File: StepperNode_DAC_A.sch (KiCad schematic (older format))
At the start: 1 part

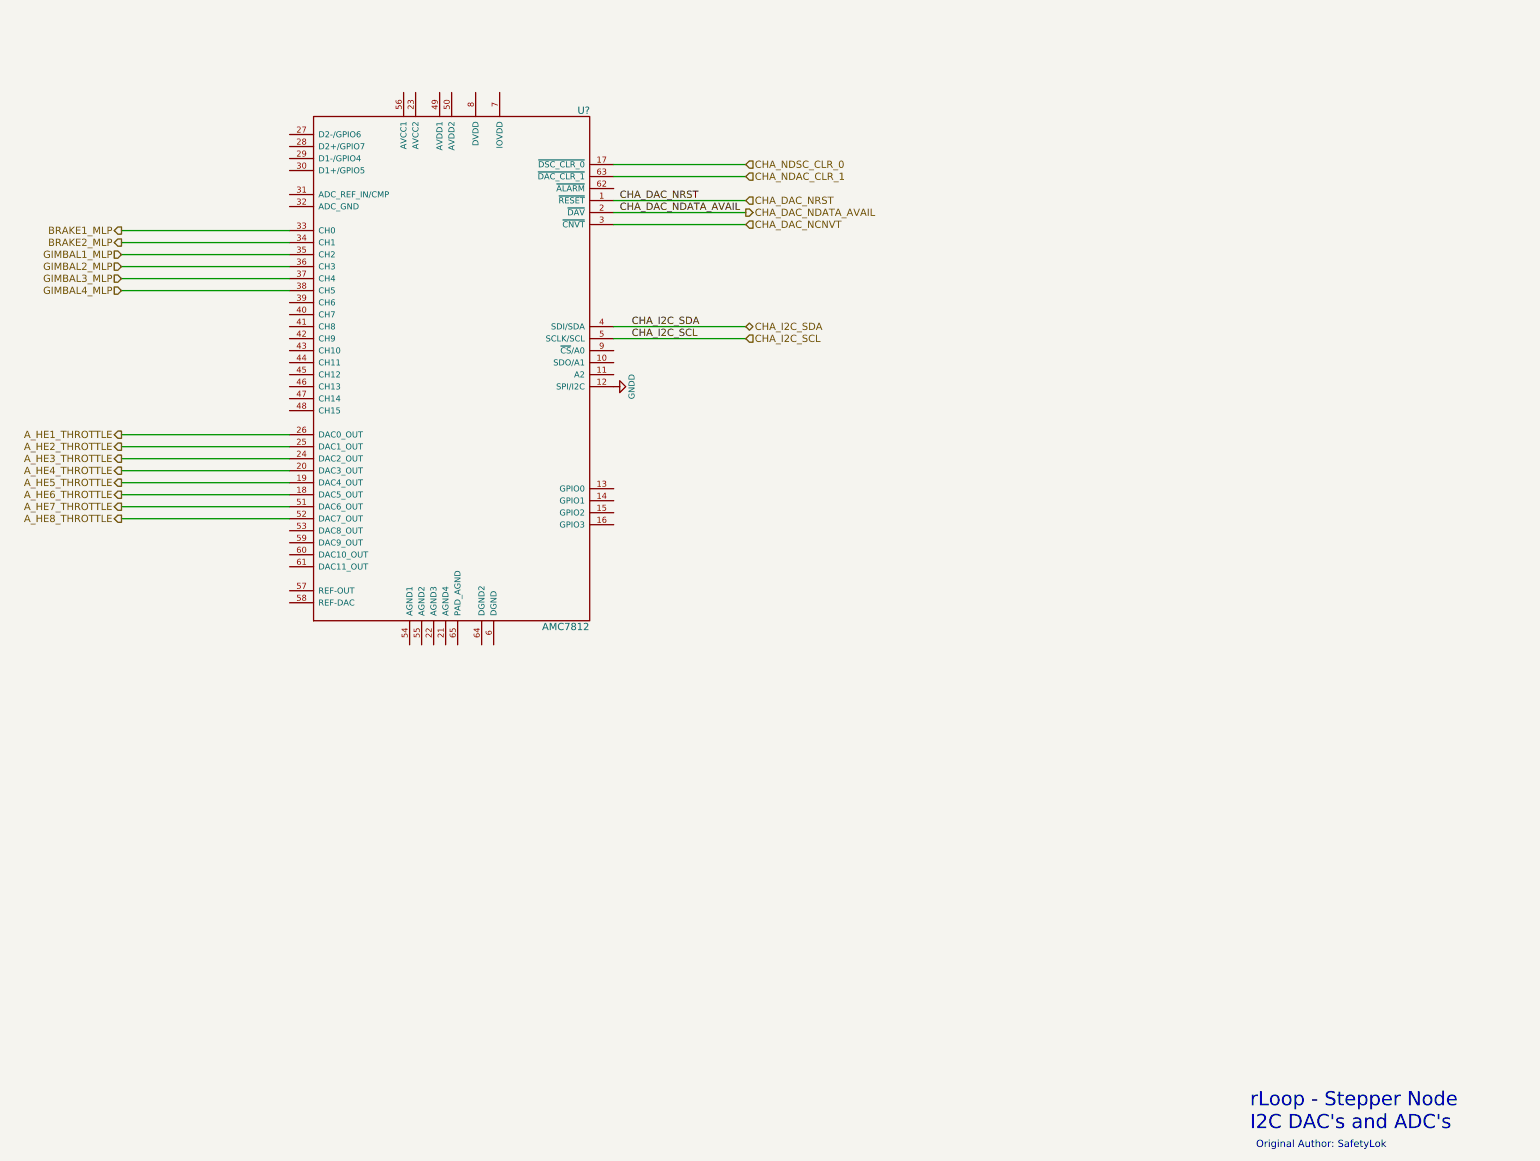
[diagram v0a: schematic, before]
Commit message: Setup DAC channel B
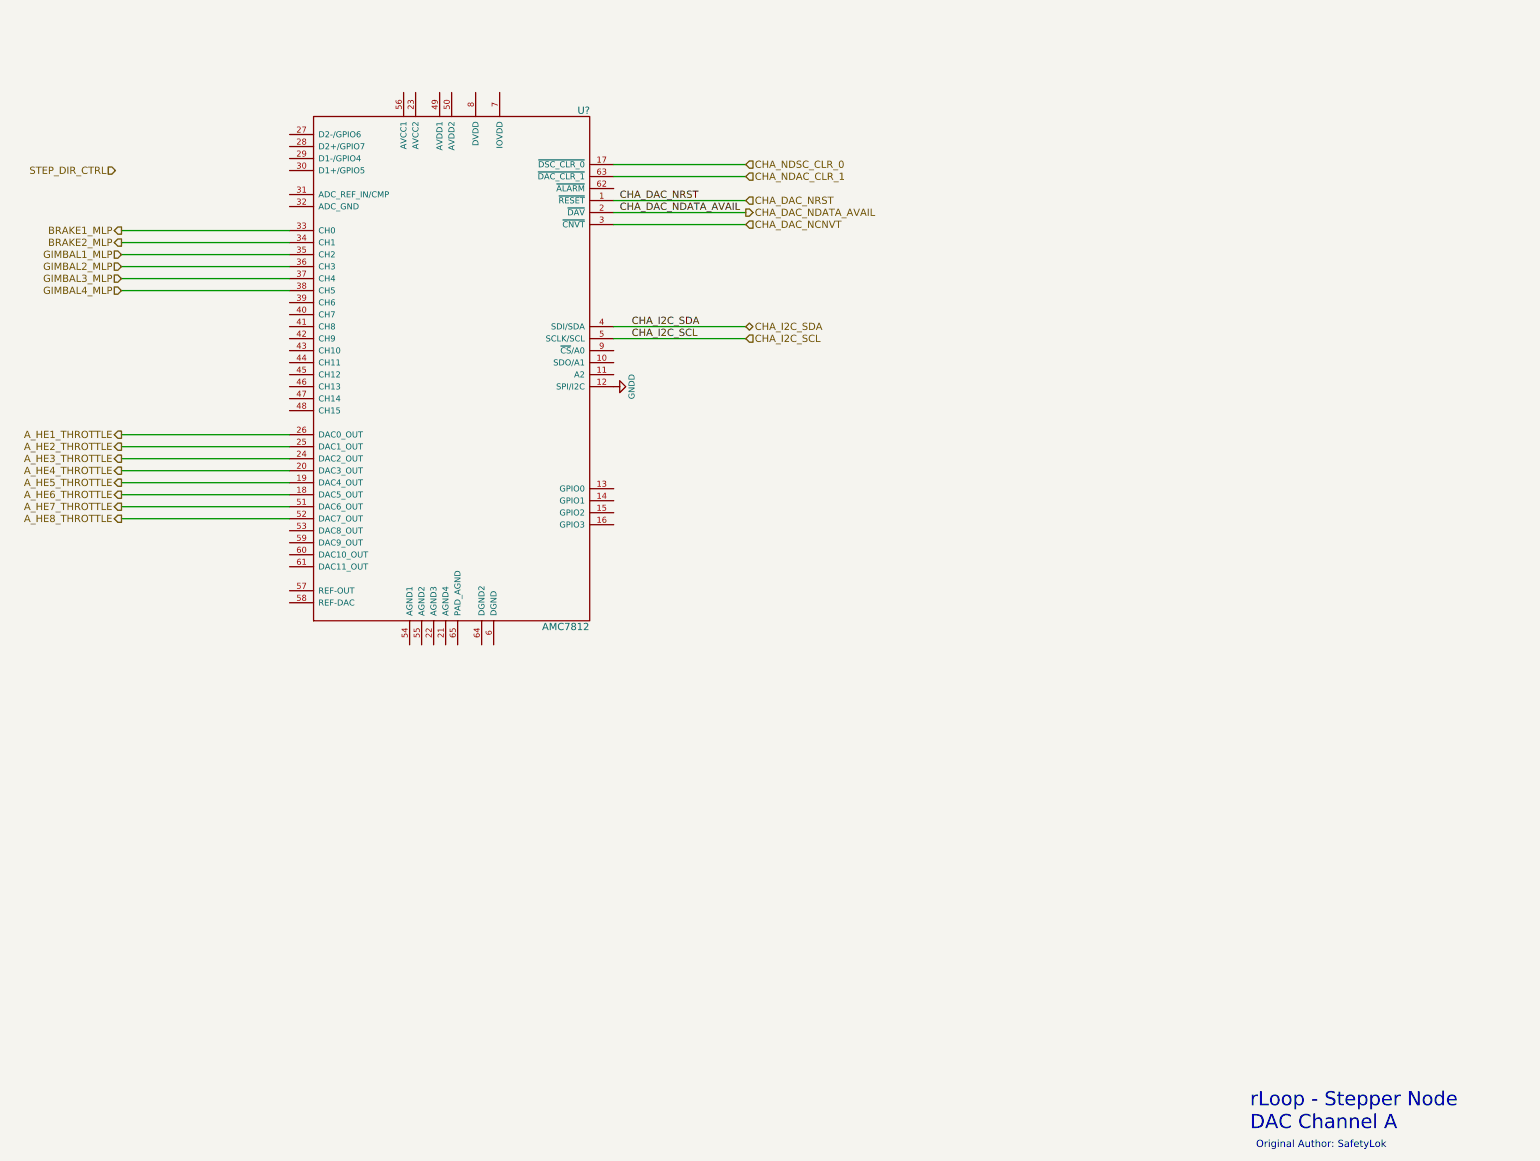
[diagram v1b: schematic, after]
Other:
- note added: "rLoop - Stepper Node\nDAC Channel A\n"
- note removed: "rLoop - Stepper Node\nI2C DAC's and ADC's\n"
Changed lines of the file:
@@
 $Descr A3 16535 11693
 encoding utf-8
-Sheet 6 8
-Title "I2C DACS and ADC's"
+Sheet 6 9
+Title "DAC Channel A"
 Date ""
 Rev "1"
@@
 $EndDescr
 Text Notes 11900 10350 0    118  ~ 0
-rLoop - Stepper Node\nI2C DAC's and ADC's\n
+rLoop - Stepper Node\nDAC Channel A\n
 Text Notes 11950 10500 0    60   ~ 0
 Original Author: SafetyLok
@@
 Wire Wire Line
 	3900 5250 2500 5250
+Text HLabel 2450 2350 0    60   Input ~ 0
+STEP_DIR_CTRL
 $EndSCHEMATC

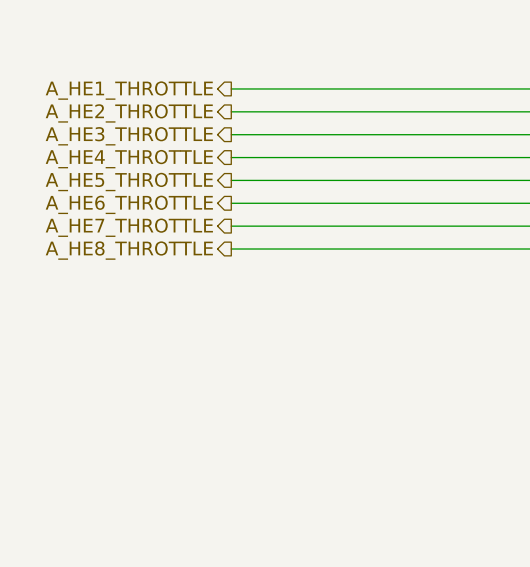
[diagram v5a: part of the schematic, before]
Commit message: Added Aux Prop Interface Sheet
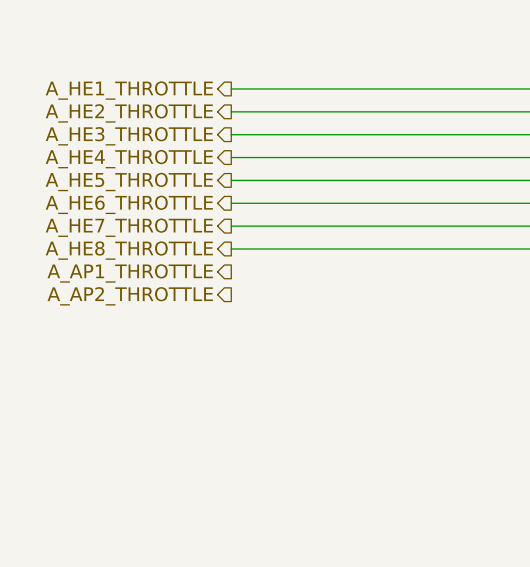
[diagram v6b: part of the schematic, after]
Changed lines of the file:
@@
 $Descr A3 16535 11693
 encoding utf-8
-Sheet 3 14
+Sheet 3 16
 Title "DAC Channel A"
 Date ""
@@
 Text HLabel 2450 2350 0    60   Input ~ 0
 STEP_DIR_CTRL
+Text HLabel 2500 5350 0    60   Output ~ 0
+A_AP1_THROTTLE
+Text HLabel 2500 5450 0    60   Output ~ 0
+A_AP2_THROTTLE
 $EndSCHEMATC

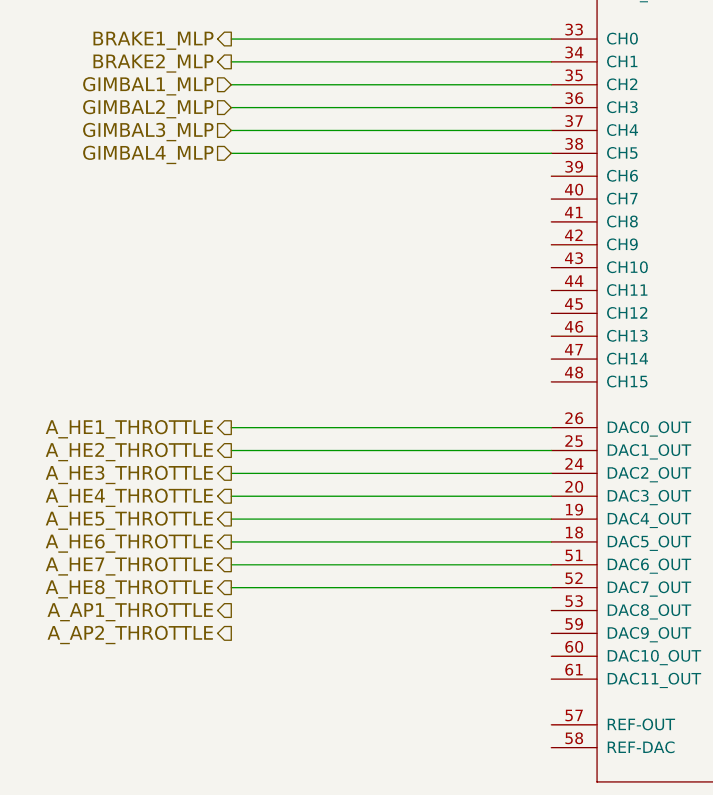
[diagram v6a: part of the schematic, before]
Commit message: Added sheet for Stepper Motor RTD temp sensors.
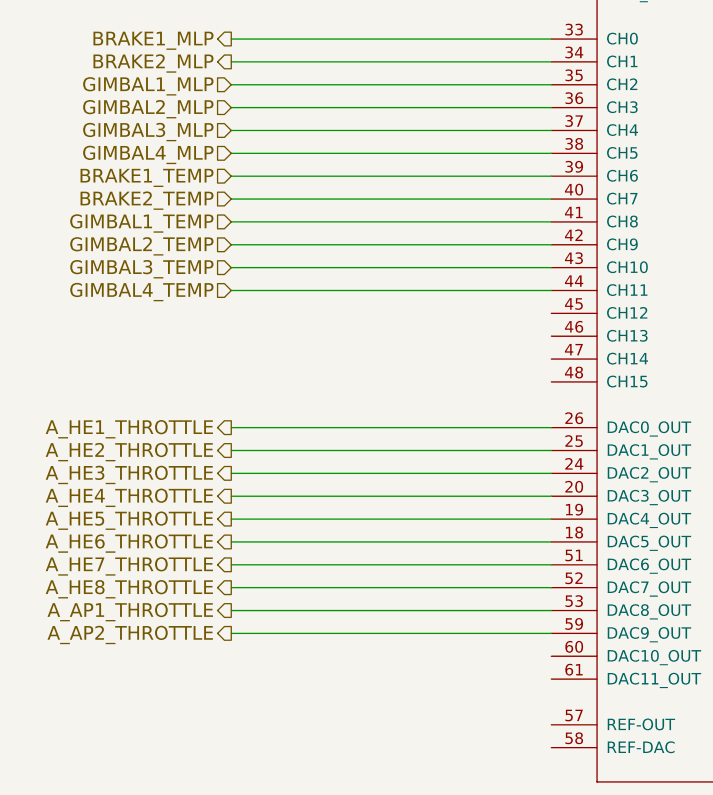
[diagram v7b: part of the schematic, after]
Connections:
- net A_AP1_THROTTLE: now also U?.53 (DAC8_OUT)
- net A_AP2_THROTTLE: now also U?.59 (DAC9_OUT)
- net BRAKE1_TEMP: now reaches U?.39 (CH6)
- net BRAKE2_TEMP: now reaches U?.40 (CH7)
- net GIMBAL1_TEMP: now reaches U?.41 (CH8)
- net GIMBAL2_TEMP: now reaches U?.42 (CH9)
- net GIMBAL3_TEMP: now reaches U?.43 (CH10)
- net GIMBAL4_TEMP: now reaches U?.44 (CH11)
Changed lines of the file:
@@
 LIBS:microcontrollers
 LIBS:dsp
-LIBS:microchip
 LIBS:analog_switches
 LIBS:motorola
@@
 $Descr A3 16535 11693
 encoding utf-8
-Sheet 3 16
+Sheet 3 17
 Title "DAC Channel A"
 Date ""
@@
 Text HLabel 2500 5450 0    60   Output ~ 0
 A_AP2_THROTTLE
+Wire Wire Line
+	3900 3450 2500 3450
+Text HLabel 2500 3450 0    60   Input ~ 0
+BRAKE1_TEMP
+Wire Wire Line
+	3900 3550 2500 3550
+Text HLabel 2500 3550 0    60   Input ~ 0
+BRAKE2_TEMP
+Wire Wire Line
+	3900 3650 2500 3650
+Text HLabel 2500 3650 0    60   Input ~ 0
+GIMBAL1_TEMP
+Wire Wire Line
+	3900 3750 2500 3750
+Text HLabel 2500 3750 0    60   Input ~ 0
+GIMBAL2_TEMP
+Wire Wire Line
+	3900 3850 2500 3850
+Text HLabel 2500 3850 0    60   Input ~ 0
+GIMBAL3_TEMP
+Wire Wire Line
+	3900 3950 2500 3950
+Text HLabel 2500 3950 0    60   Input ~ 0
+GIMBAL4_TEMP
+Wire Wire Line
+	3900 5350 2500 5350
+Wire Wire Line
+	2500 5450 3900 5450
 $EndSCHEMATC

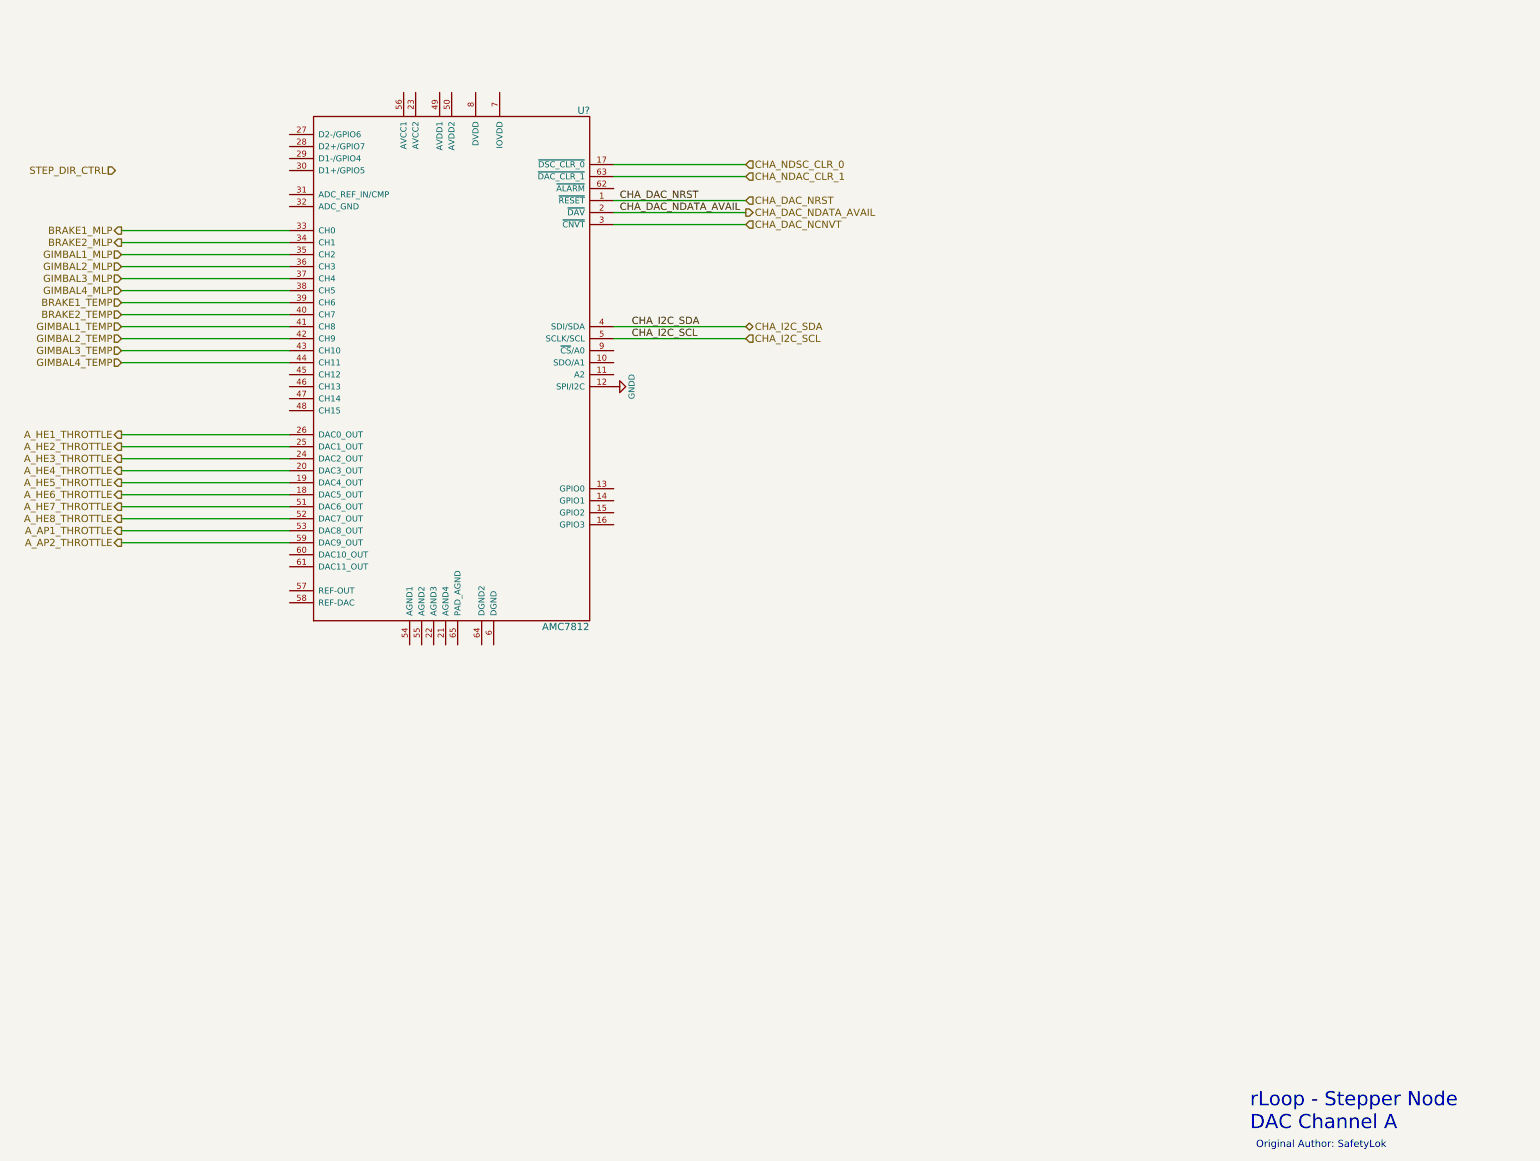
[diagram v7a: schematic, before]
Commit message: Finished DAC interface sheets.
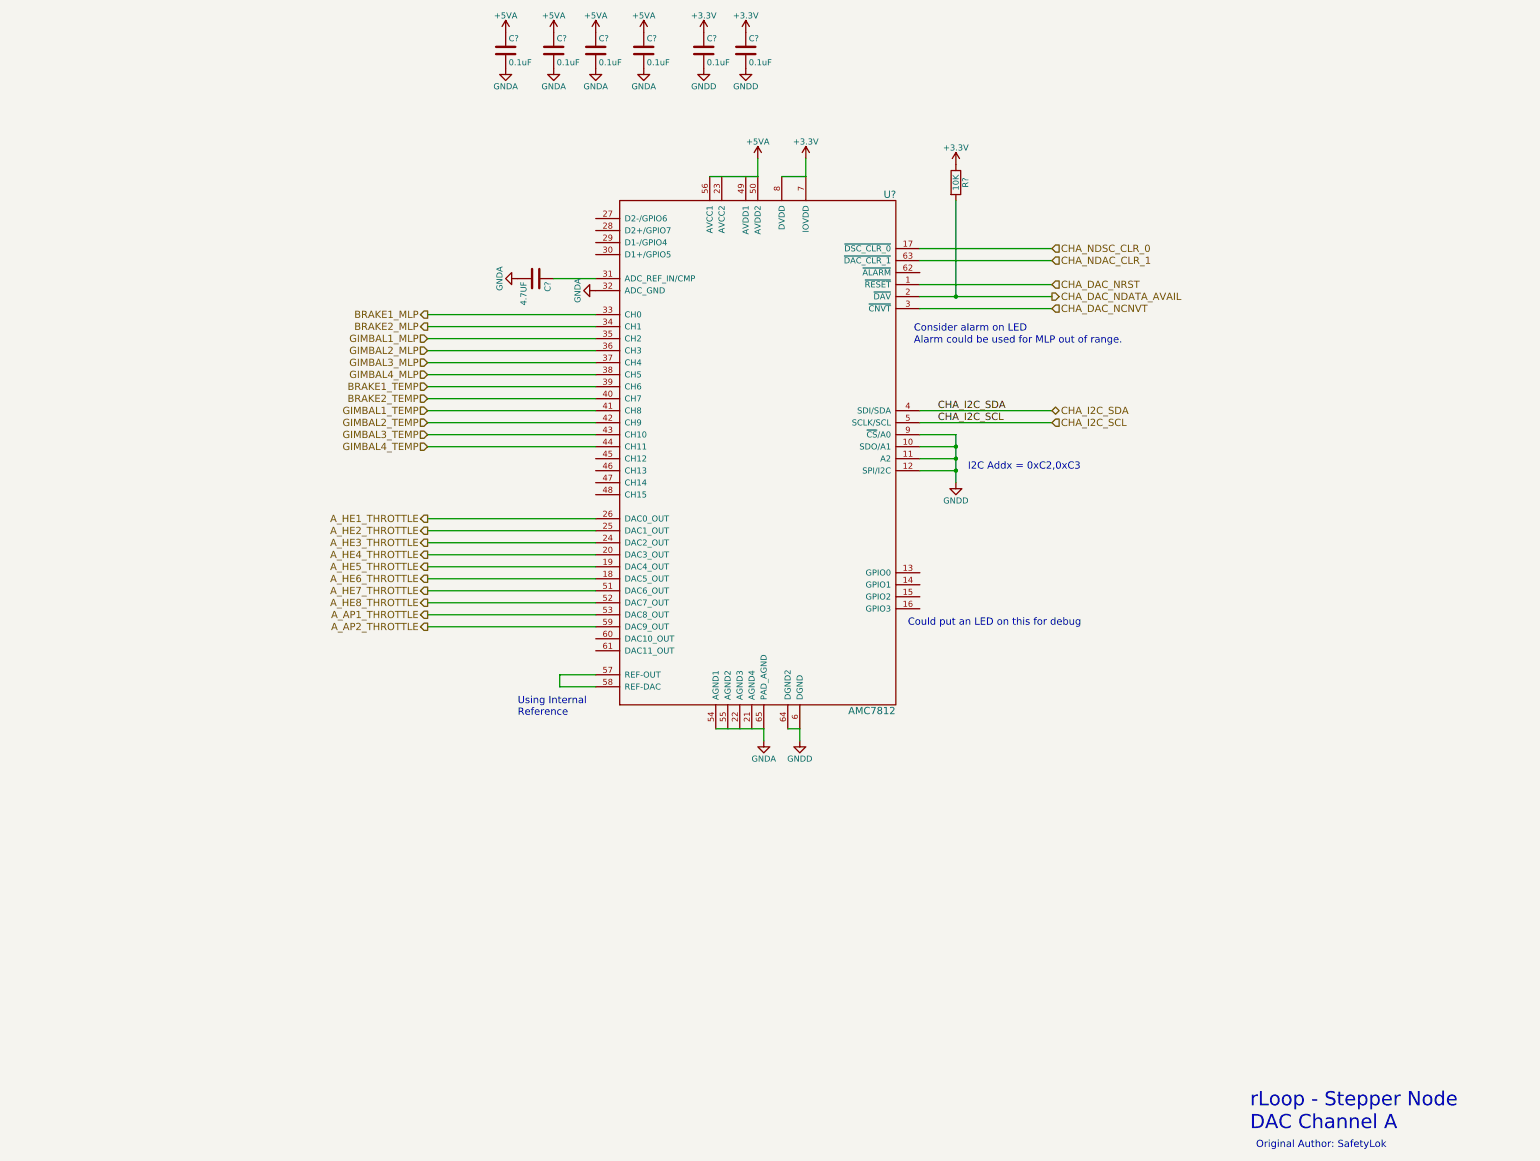
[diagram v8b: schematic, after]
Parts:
- added C?: 4.7UF, symbol C
- added C? (x6): 0.1uF, symbol C
- added R?: 10K, symbol R
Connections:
- net CHA_DAC_NDATA_AVAIL: now also R?.2
- net GNDD: now also U?.10 (SDO/A1), U?.11 (A2), U?.6 (DGND), U?.64 (DGND2), U?.9 (~CS~/A0), C?.2, C?.2
- net at U?.31 (ADC_REF_IN/CMP): now also C?.1
- net GNDA: now reaches U?.32 (ADC_GND)
- net GNDA: now also U?.54 (AGND1), U?.65 (PAD_AGND), C?.2, C?.2, C?.2, C?.2, C?.2
- net +5VA: now reaches U?.50 (AVDD2)
- net +5VA: now also U?.56 (AVCC1), C?.1, C?.1, C?.1, C?.1
- net at U?.57 (REF-OUT): now also U?.58 (REF-DAC)
- net +3V3: now reaches U?.7 (IOVDD)
- net +3V3: now also U?.8 (DVDD), C?.1, C?.1, R?.1
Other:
- note added: "Alarm could be used for MLP out of range."
- note added: "Consider alarm on LED"
- note added: "Could put an LED on this for debug"
- note added: "I2C Addx = 0xC2,0xC3"
- note added: "Using Internal\nReference"
- moved on the sheet: U?
